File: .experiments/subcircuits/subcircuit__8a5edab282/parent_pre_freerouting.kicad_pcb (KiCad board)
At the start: 2 copper layers, 270.5 x 111.3 mm, 39 parts, among them J1 USB_C, J2 Output, J3 Debug, Q1 FS8205A, U1 USBLC6-2SC6, U2 BQ24072, U3 HY2113-KB5B, U4 MT3608, U5 AP2112K-3.3, U6 LN61CN3302MR-G

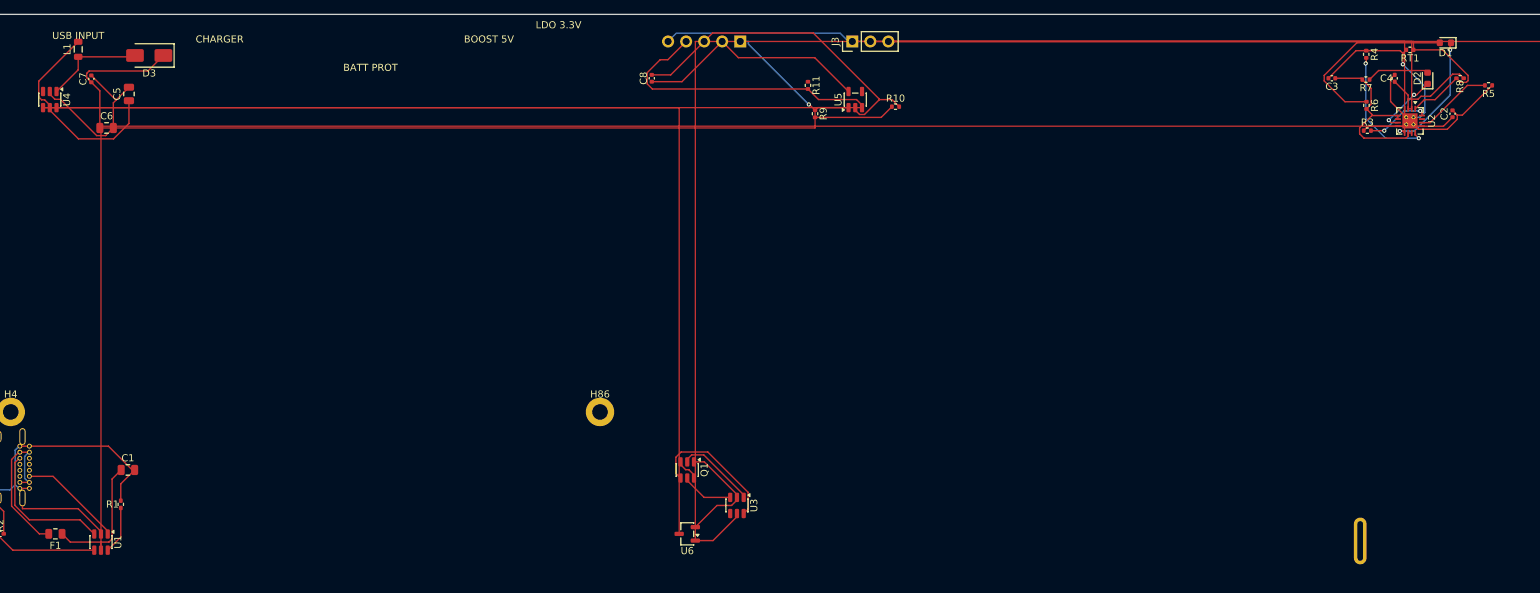
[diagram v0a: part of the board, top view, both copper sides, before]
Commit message: feat: unified hierarchical solver (solve_hierarchy.py)
Single-command entry point for the full subcircuit pipeline:
  python3 solve_hierarchy.py LLUPS.kicad_sch --pcb LLUPS.kicad_pcb --route

Phase 1: Solve leaf subcircuits (delegates to solve_subcircuits.py)
  - 6 leaves solved and routed via FreeRouting
  - Canonical copper persisted in solved_layout.json

Phase 2: Compose and route parent (delegates to compose_subcircuits.py)
  - Grid layout of 6 children with 5mm spacing
  - Child copper preserved on stamped parent board
  - FreeRouting routes interconnect nets between subcircuits
  - Parent artifact persisted with full copper

Flags: --skip-leaves, --leaf-only, --rounds, --mode, --spacing-mm, --jar
Full pipeline completes in ~4 minutes (with routing)
Skip-leaves mode completes in ~28 seconds
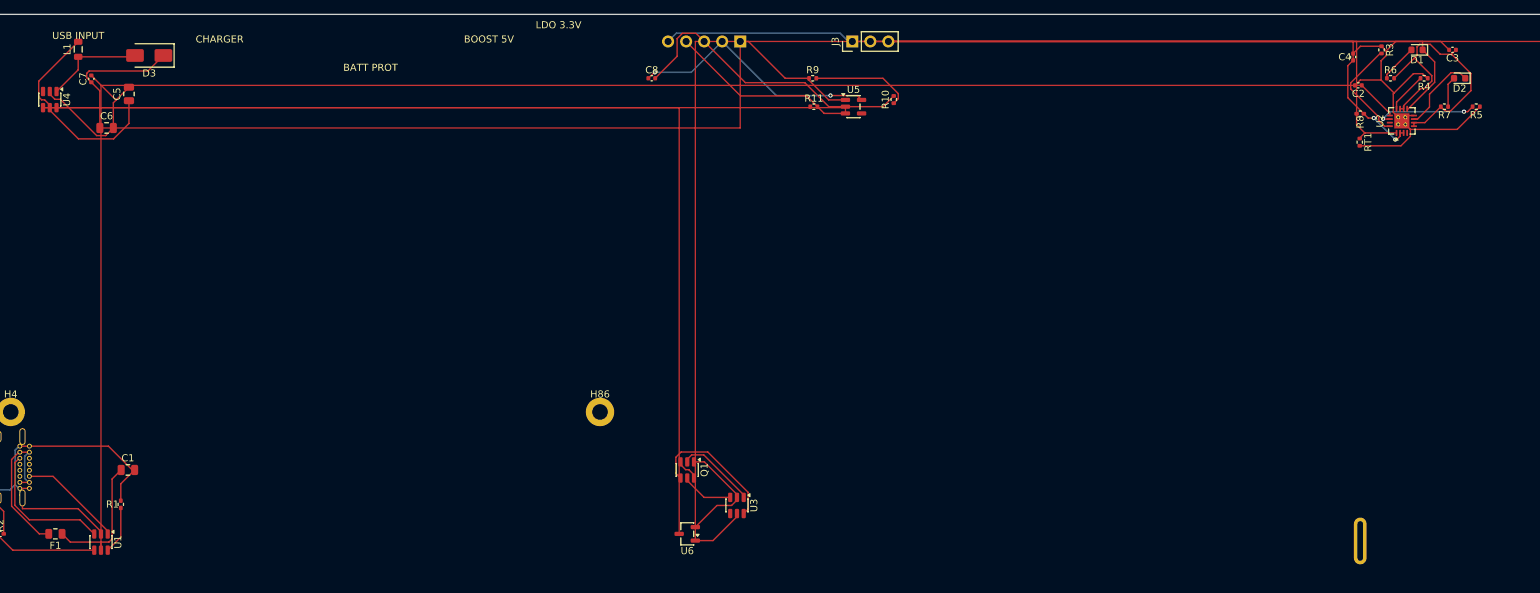
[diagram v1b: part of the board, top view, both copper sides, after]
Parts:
- moved C3 17.5 mm to (206.6, 4.00)
- moved R8 14.9 mm to (193.6, 13.0)
- moved RT1 14.8 mm to (193.5, 17.0), turned to -90 degrees
- moved C2 13.9 mm to (193.3, 9.00), turned to 180 degrees
- moved R7 11.7 mm to (205.4, 12.0)
- moved R3 11.6 mm to (196.6, 4.00), turned to -90 degrees
- moved R4 8.83 mm to (202.6, 8.00), turned to 180 degrees
- moved C4 6.58 mm to (192.6, 5.00)
- moved R6 5.10 mm to (197.8, 8.00), turned to 0 degrees
- moved R9 5.01 mm to (116.5, 8.00), turned to 0 degrees
- moved D2 4.51 mm to (207.6, 8.00), turned to 180 degrees
- moved D1 4.12 mm to (201.6, 4.00)
- moved R5 3.46 mm to (209.9, 12.0)
- moved R11 3.11 mm to (116.6, 12.0), turned to 0 degrees
- moved U2 1.14 mm to (199.4, 14.0), turned to 90 degrees
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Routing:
- net (no net): track 1194.9 -> 1166.5 mm
- net Net-(D1-A): track 26.1 -> 5.43 mm
- net /VSYS: track 25.6 -> 40.0 mm
- net /EN: track 40.7 -> 26.6 mm
- net Net-(U2-ILIM): track 18.1 -> 5.70 mm, vias 2 -> 0
- net /NTC_SENSE: track 19.5 -> 8.73 mm
- net /CHG_N: track 17.4 -> 10.7 mm, vias 2 -> 0
- net Net-(U2-ISET): track 8.84 -> 14.9 mm, vias 2 -> 0
- net Net-(D2-A): track 8.83 -> 4.35 mm
- net Net-(U2-TMR): track 11.0 -> 14.3 mm, vias 0 -> 2
- net /3V3: track 33.0 -> 35.6 mm, vias 0 -> 2
- net Net-(U4-FB): track 11.5 -> 14.1 mm
- net Net-(D2-K): track 9.01 -> 11.3 mm, vias 2 -> 0
- net /VBAT: track 49.8 -> 51.7 mm, vias 0 -> 2
- net /5V: track 39.9 -> 38.7 mm, vias 1 -> 0
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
